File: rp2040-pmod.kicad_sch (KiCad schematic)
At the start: 42 parts, among them J1 USB_C_Receptacle_USB2.0, J2 Conn_01x03, J3 Conn_02x06_Odd_Even, SW1 USB Boot, SW2 USER1, SW3 RESET, U1 W25Q32JVSS, U2 AP2112K-3.3, U3 LM66200, U4 RP2040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

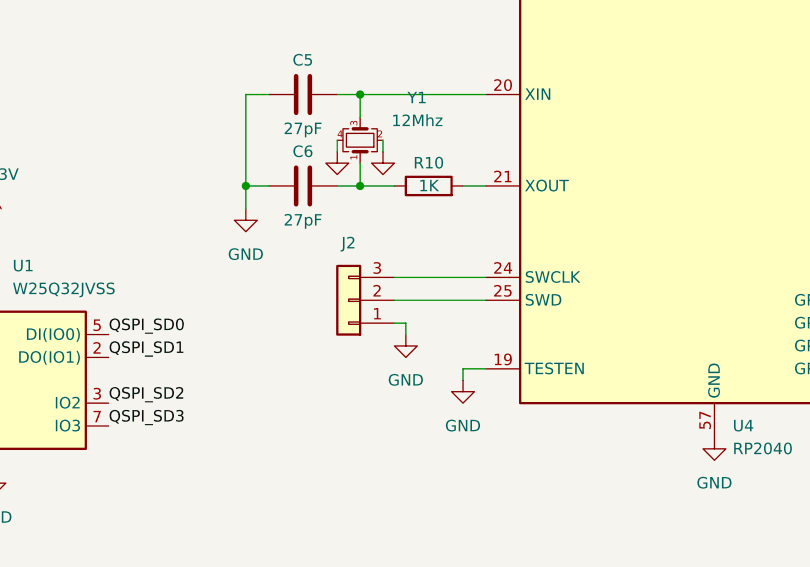
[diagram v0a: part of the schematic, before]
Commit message: Switch to .1" debug header
Also add some silkscreen labels on the bottom.
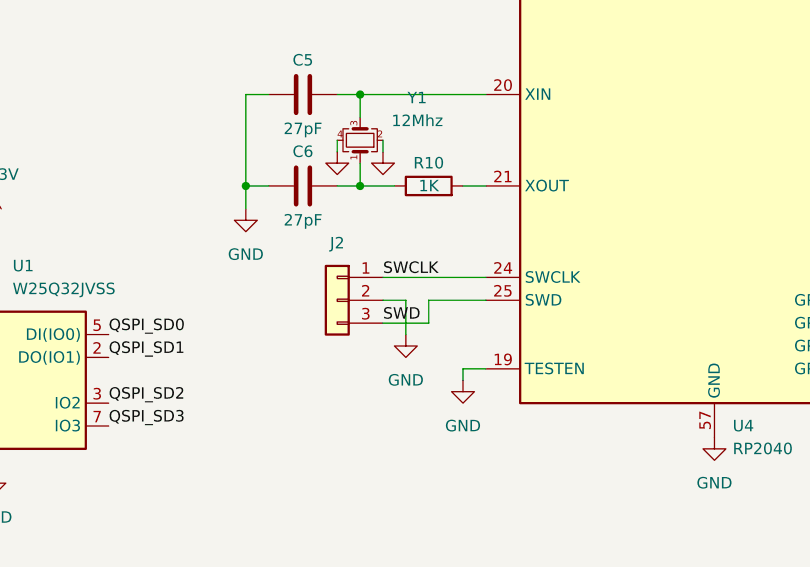
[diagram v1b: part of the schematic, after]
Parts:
- J2: footprint Connector_PinHeader_1.27mm:PinHeader_1x03_P1.27mm_Vertical -> Connector_PinHeader_2.54mm:PinHeader_1x03_P2.54mm_Vertical
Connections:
- net GND: now also J2.2 (Pin_2); no longer J2.1 (Pin_1)
- net SWCLK: now reaches U4.24 (SWCLK)
- net SWCLK: now also J2.1 (Pin_1); no longer J2.3 (Pin_3)
- net SWD: now reaches U4.25 (SWD)
- net SWD: now also J2.3 (Pin_3); no longer J2.2 (Pin_2)
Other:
- moved on the sheet: J2
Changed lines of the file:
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@@
+    (stroke (width 0) (type default) (color 0 0 0 0))
+  )
+  (wire (pts (xy 113.03 125.73) (xy 113.03 123.19))
     (stroke (width 0) (type default) (color 0 0 0 0))
   )
@@
     (stroke (width 0) (type default) (color 0 0 0 0))
   )
+  (wire (pts (xy 110.49 123.19) (xy 107.95 123.19))
+    (stroke (width 0) (type default) (color 0 0 0 0))
+  )
   (wire (pts (xy 115.57 54.61) (xy 118.11 54.61))
     (stroke (width 0) (type default) (color 0 0 0 0))
@@
     (stroke (width 0) (type default) (color 0 0 0 0))
   )
-  (wire (pts (xy 110.49 125.73) (xy 110.49 127))
+  (wire (pts (xy 110.49 123.19) (xy 110.49 127))
     (stroke (width 0) (type default) (color 0 0 0 0))
   )
@@
     (stroke (width 0) (type default) (color 0 0 0 0))
   )
+  (wire (pts (xy 113.03 123.19) (xy 119.38 123.19))
+    (stroke (width 0) (type default) (color 0 0 0 0))
+  )
   (wire (pts (xy 135.89 167.64) (xy 142.24 167.64))
     (stroke (width 0) (type default) (color 0 0 0 0))
@@
     (stroke (width 0) (type default) (color 0 0 0 0))
   )
-  (wire (pts (xy 109.22 123.19) (xy 119.38 123.19))
-    (stroke (width 0) (type default) (color 0 0 0 0))
-  )
   (wire (pts (xy 199.39 116.84) (xy 199.39 115.57))
     (stroke (width 0) (type default) (color 0 0 0 0))
@@
     (stroke (width 0) (type default) (color 0 0 0 0))
   )
+  (wire (pts (xy 107.95 120.65) (xy 119.38 120.65))
+    (stroke (width 0) (type default) (color 0 0 0 0))
+  )
   (wire (pts (xy 196.85 31.75) (xy 207.01 31.75))
     (stroke (width 0) (type default) (color 0 0 0 0))
@@
     (stroke (width 0) (type default) (color 0 0 0 0))
   )
+  (wire (pts (xy 107.95 125.73) (xy 113.03 125.73))
+    (stroke (width 0) (type default) (color 0 0 0 0))
+  )
   (wire (pts (xy 49.53 129.54) (xy 52.07 129.54))
     (stroke (width 0) (type default) (color 0 0 0 0))
@@
     (stroke (width 0) (type default) (color 0 0 0 0))
   )
-  (wire (pts (xy 109.22 125.73) (xy 110.49 125.73))
-    (stroke (width 0) (type default) (color 0 0 0 0))
-  )
   (wire (pts (xy 217.17 31.75) (xy 228.6 31.75))
     (stroke (width 0) (type default) (color 0 0 0 0))
@@
   )
   (wire (pts (xy 20.32 121.92) (xy 19.05 121.92))
-    (stroke (width 0) (type default) (color 0 0 0 0))
-  )
-  (wire (pts (xy 109.22 120.65) (xy 119.38 120.65))
     (stroke (width 0) (type default) (color 0 0 0 0))
   )
@@
     (effects (font (size 1.27 1.27)) (justify left bottom))
   )
+  (label "SWCLK" (at 107.95 120.65 0)
+    (effects (font (size 1.27 1.27)) (justify left bottom))
+  )
   (label "GPIO1" (at 181.61 57.15 0)
     (effects (font (size 1.27 1.27)) (justify left bottom))
@@
   (label "GPIO6" (at 223.52 62.23 180)
     (effects (font (size 1.27 1.27)) (justify right bottom))
+  )
+  (label "SWD" (at 107.95 125.73 0)
+    (effects (font (size 1.27 1.27)) (justify left bottom))
   )
   (label "GPIO7" (at 236.22 62.23 0)
@@
     (pin "5")
   )
-  (symbol (lib_id "Connector_Generic:Conn_01x03") (at 104.14 123.19 180) (unit 1)
-    (in_bom yes) (on_board yes) (fields_autoplaced)
-    (property "Reference" "J2" (id 0) (at 104.14 116.84 0))
-    (property "Value" "Conn_01x03" (id 1) (at 104.14 116.84 0)
-      (effects (font (size 1.27 1.27)) hide)
-    )
-    (property "Footprint" "Connector_PinHeader_1.27mm:PinHeader_1x03_P1.27mm_Vertical" (id 2) (at 104.14 123.19 0)
-      (effects (font (size 1.27 1.27)) hide)
-    )
-    (property "Datasheet" "~" (id 3) (at 104.14 123.19 0)
+  (symbol (lib_id "Connector_Generic:Conn_01x03") (at 102.87 123.19 0) (mirror y) (unit 1)
+    (in_bom yes) (on_board yes) (fields_autoplaced)
+    (property "Reference" "J2" (id 0) (at 102.87 116.84 0))
+    (property "Value" "Conn_01x03" (id 1) (at 102.87 129.54 0)
+      (effects (font (size 1.27 1.27)) hide)
+    )
+    (property "Footprint" "Connector_PinHeader_2.54mm:PinHeader_1x03_P2.54mm_Vertical" (id 2) (at 102.87 123.19 0)
+      (effects (font (size 1.27 1.27)) hide)
+    )
+    (property "Datasheet" "~" (id 3) (at 102.87 123.19 0)
       (effects (font (size 1.27 1.27)) hide)
     )
@@
     )
     (path "/f069dead-41d5-463b-a95e-8ec98b7a13ad"
-      (reference "J2") (unit 1) (value "Conn_01x03") (footprint "Connector_PinHeader_1.27mm:PinHeader_1x03_P1.27mm_Vertical")
+      (reference "J2") (unit 1) (value "Conn_01x03") (footprint "Connector_PinHeader_2.54mm:PinHeader_1x03_P2.54mm_Vertical")
     )
     (path "/95c3f47f-3388-4a49-a488-a3e069372db9"

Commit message: Update LM66200 footprint
The footprint used was the wrong pitch and width. :(
New footprint is close enough to the datasheet to actually work. :)
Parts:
- U3: footprint Package_TO_SOT_SMD:SOT-23-8 -> rp2040-pmod:SOT-5x3
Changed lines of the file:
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@@
     (property "Reference" "U3" (id 0) (at 125.73 160.02 0))
     (property "Value" "LM66200" (id 1) (at 125.73 162.56 0))
-    (property "Footprint" "Package_TO_SOT_SMD:SOT-23-8" (id 2) (at 118.11 170.18 0)
+    (property "Footprint" "rp2040-pmod:SOT-5x3" (id 2) (at 118.11 170.18 0)
       (effects (font (size 1.27 1.27)) hide)
     )
@@
     )
     (path "/ee73be83-5e82-409b-99e7-fda6995d341e"
-      (reference "U3") (unit 1) (value "LM66200") (footprint "Package_TO_SOT_SMD:SOT-23-8")
+      (reference "U3") (unit 1) (value "LM66200") (footprint "rp2040-pmod:SOT-5x3")
     )
     (path "/c0c35ed2-d732-4ad4-b5d7-3ffd5a246f75"

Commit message: Switch flash, add ADC header, add PMOD power detection
USON pattern swiped from emeb's library.

https://github.com/emeb/KiCad_Libs
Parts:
- added J4: Conn_01x06, Connector_PinHeader_2.54mm:PinHeader_1x06_P2.54mm_Vertical, symbol Connector_Generic:Conn_01x06
- added R12: 10K, Resistor_SMD:R_0402_1005Metric, symbol Device:R
- U1: value W25Q32JVSS -> W25Q16JVUXIQ; footprint Package_SO:SOIC-8_5.23x5.23mm_P1.27mm -> rp2040-pmod:USON-8_2x3
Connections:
- net +3.3V: now also J4.5 (Pin_5)
- net +3.3VP: now also R12.2
- net GND: now also J4.6 (Pin_6)
- net at U4.15 (GPIO12): now also R12.1
- net ADC0: now reaches U4.38 (GPIO26_ADC0)
- net ADC0: now also J4.1 (Pin_1)
- net ADC1: now reaches U4.39 (GPIO27_ADC1)
- net ADC1: now also J4.2 (Pin_2)
- net ADC2: now reaches U4.40 (GPIO28_ADC2)
- net ADC2: now also J4.3 (Pin_3)
- net ADC3: now reaches U4.41 (GPIO29_ADC3)
- net ADC3: now also J4.4 (Pin_4)
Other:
- moved on the sheet: D1, R11, SW2
